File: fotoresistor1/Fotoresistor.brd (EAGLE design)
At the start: 68.6 x 53.3 mm, 4 parts

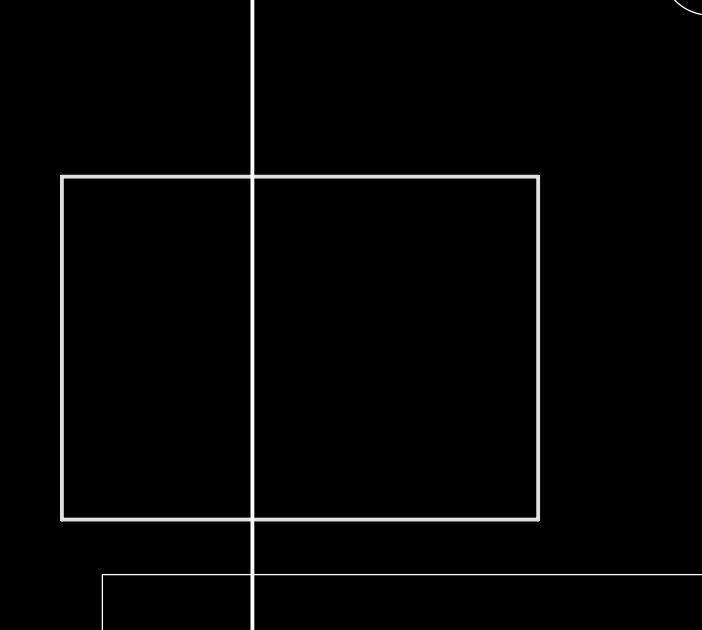
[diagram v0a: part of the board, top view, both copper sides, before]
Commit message: corrección de la conexión del foto resistor --> ahora anda
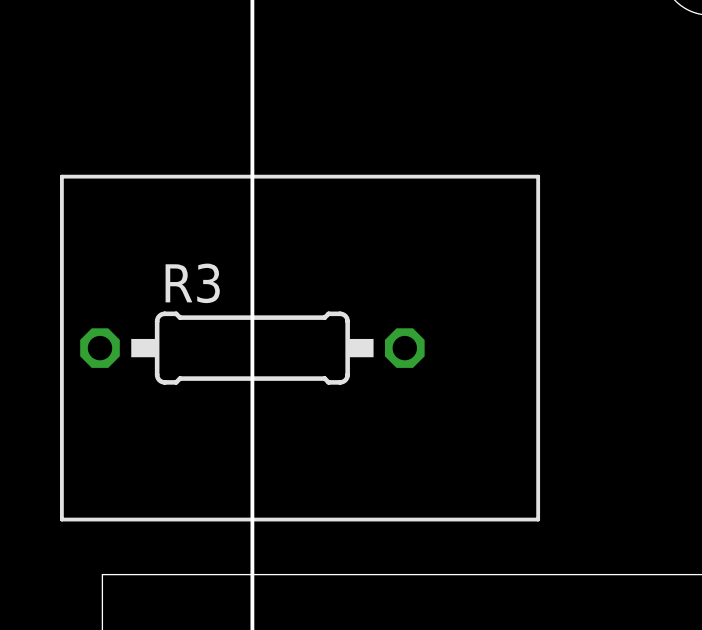
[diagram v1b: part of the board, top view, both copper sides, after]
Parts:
- added R3: 330‎Ω, AUTODESK_CIRCUITS_BREADBOARD:0207/10
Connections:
- removed net N$2 (its old number): R1.P$2, U1.A0
- new net N$4: R1.P$1, R2.1, U1.GND..
- net N$1: now also R3.1; no longer R1.P$1
- net N$5: now also R1.P$2, R3.2, U1.A0; no longer R2.1, U1.GND..
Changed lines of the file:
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@@
 </autorouter>
 <elements>
-<element value="" name="R1" library="AUTODESK_CIRCUITS_BREADBOARD" package="PHOTORESISTOR-2.54" x="5" y="10.08"></element><element value="" name="U1" library="AUTODESK_CIRCUITS_BREADBOARD" package="ARDUINO_UNO" x="5" y="22.78"></element><element value="" name="D2" library="AUTODESK_CIRCUITS_BREADBOARD" package="LED5MM" x="5" y="35.480000000000004"></element><element value="220‎Ω" name="R2" library="AUTODESK_CIRCUITS_BREADBOARD" package="0207/10" x="5" y="48.18"></element></elements>
+<element value="" name="R1" library="AUTODESK_CIRCUITS_BREADBOARD" package="PHOTORESISTOR-2.54" x="5" y="10.08"></element><element value="" name="U1" library="AUTODESK_CIRCUITS_BREADBOARD" package="ARDUINO_UNO" x="5" y="22.78"></element><element value="" name="D2" library="AUTODESK_CIRCUITS_BREADBOARD" package="LED5MM" x="5" y="35.480000000000004"></element><element value="220‎Ω" name="R2" library="AUTODESK_CIRCUITS_BREADBOARD" package="0207/10" x="5" y="48.18"></element><element value="330‎Ω" name="R3" library="AUTODESK_CIRCUITS_BREADBOARD" package="0207/10" x="5" y="60.879999999999995"></element></elements>
 <signals>
-<signal name="N$1"><contactref element="U1" pad="5V"></contactref><contactref element="R1" pad="P$1"></contactref><wire x1="43.1" y1="25.32" x2="3.73" y2="10.08" width="0" layer="19" extent="1-1"></wire></signal><signal name="N$2"><contactref element="R1" pad="P$2"></contactref><contactref element="U1" pad="A0"></contactref><wire x1="6.27" y1="10.08" x2="55.8" y2="25.32" width="0" layer="19" extent="1-1"></wire></signal><signal name="N$3"><contactref element="D2" pad="K"></contactref><contactref element="R2" pad="2"></contactref><wire x1="6.27" y1="35.480000000000004" x2="10.08" y2="48.18" width="0" layer="19" extent="1-1"></wire></signal><signal name="N$4"><contactref element="D2" pad="A"></contactref><contactref element="U1" pad="13"></contactref><wire x1="3.73" y1="35.480000000000004" x2="33.956" y2="73.58" width="0" layer="19" extent="1-1"></wire></signal><signal name="N$5"><contactref element="R2" pad="1"></contactref><contactref element="U1" pad="GND.."></contactref><wire x1="-0.08000000000000007" y1="48.18" x2="45.64" y2="25.32" width="0" layer="19" extent="1-1"></wire></signal></signals>
+<signal name="N$1"><contactref element="U1" pad="5V"></contactref><contactref element="R3" pad="1"></contactref><wire x1="43.1" y1="25.32" x2="-0.08000000000000007" y2="60.879999999999995" width="0" layer="19" extent="1-1"></wire></signal><signal name="N$2"><contactref element="D2" pad="K"></contactref><contactref element="R2" pad="2"></contactref><wire x1="6.27" y1="35.480000000000004" x2="10.08" y2="48.18" width="0" layer="19" extent="1-1"></wire></signal><signal name="N$3"><contactref element="D2" pad="A"></contactref><contactref element="U1" pad="13"></contactref><wire x1="3.73" y1="35.480000000000004" x2="33.956" y2="73.58" width="0" layer="19" extent="1-1"></wire></signal><signal name="N$4"><contactref element="R2" pad="1"></contactref><contactref element="U1" pad="GND.."></contactref><wire x1="-0.08000000000000007" y1="48.18" x2="45.64" y2="25.32" width="0" layer="19" extent="1-1"></wire><contactref element="R1" pad="P$1"></contactref><wire x1="45.64" y1="25.32" x2="3.73" y2="10.08" width="0" layer="19" extent="1-1"></wire></signal><signal name="N$5"><contactref element="R1" pad="P$2"></contactref><contactref element="R3" pad="2"></contactref><wire x1="6.27" y1="10.08" x2="10.08" y2="60.879999999999995" width="0" layer="19" extent="1-1"></wire><contactref element="U1" pad="A0"></contactref><wire x1="10.08" y1="60.879999999999995" x2="55.8" y2="25.32" width="0" layer="19" extent="1-1"></wire></signal></signals>
 </board>
 </drawing>
